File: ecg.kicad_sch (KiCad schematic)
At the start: 37 parts, among them SW1 SW_Push, SW2 SW_Push, U1 ESP32-S3-PICO-1-N8R2, U2 AD620, U3 OPA358, U4 TPS7A8101DRBR

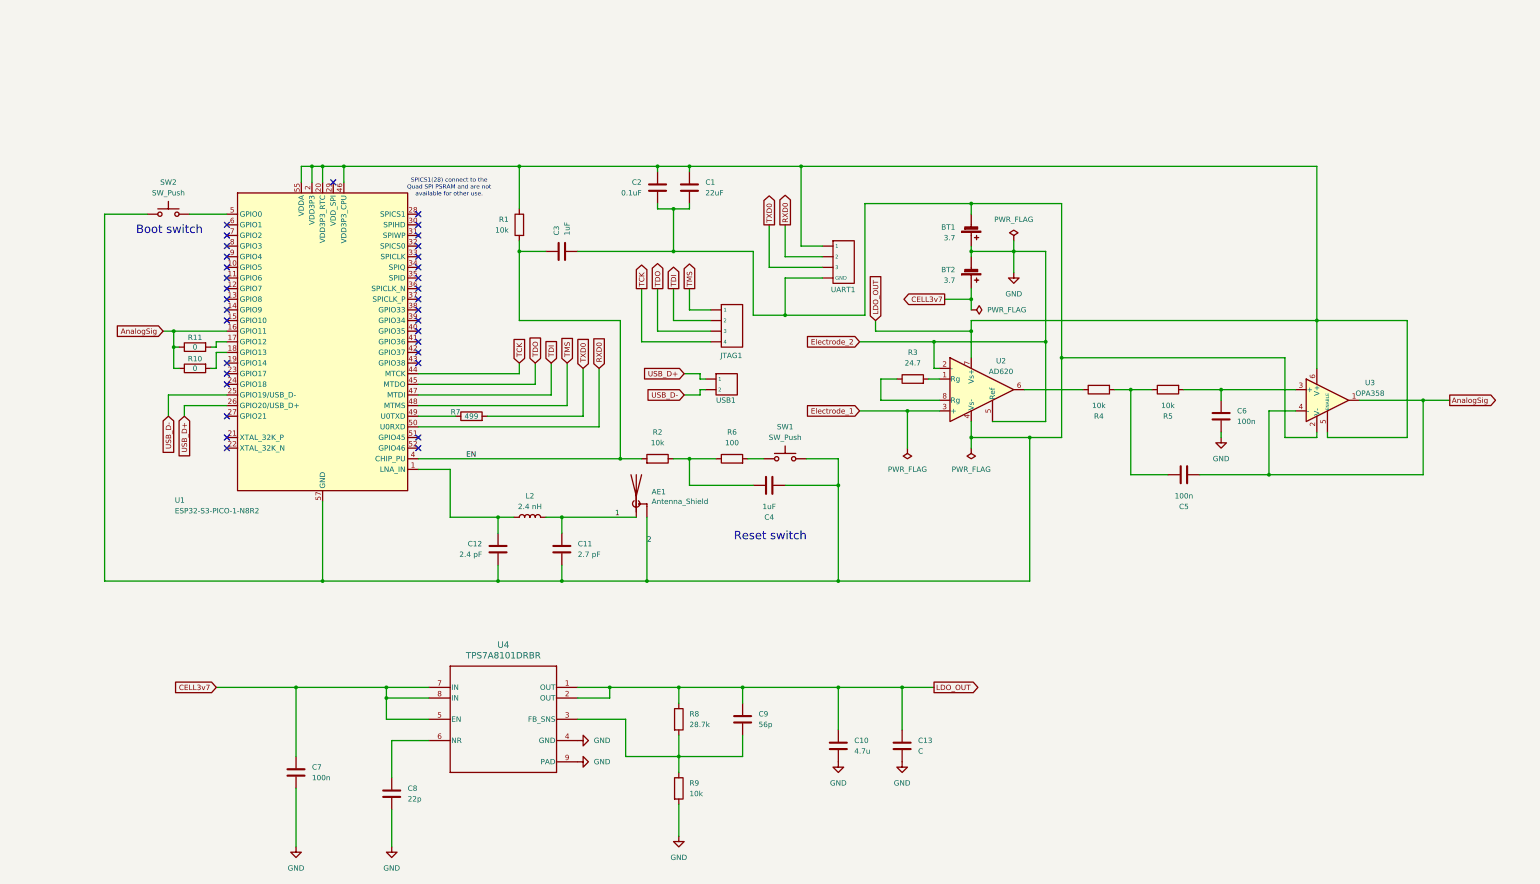
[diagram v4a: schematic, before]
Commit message: Up to date with Final PCB sent for fabrication
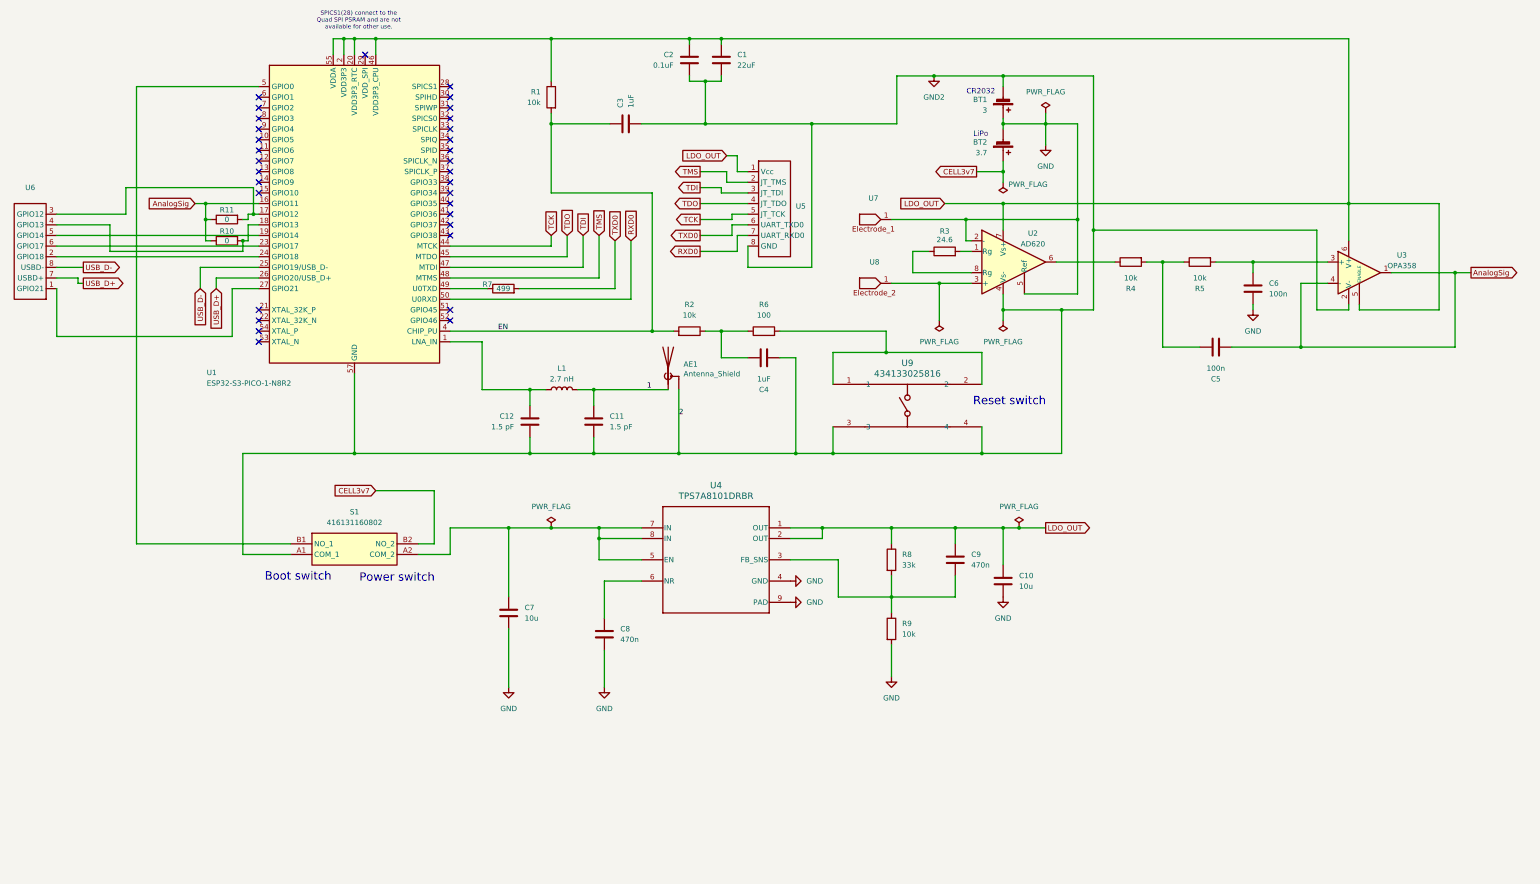
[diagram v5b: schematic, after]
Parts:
- removed C13: C, Capacitor_SMD:C_0201_0603Metric, symbol Device:C
- removed JTAG1: ~, symbol jtag:JTAG_Blackbox
- removed SW1, SW2: SW_Push, Button_Switch_THT:SW_PUSH_6mm_H5mm, symbol Switch:SW_Push
- removed UART1: ~, symbol uart:UART_Blackbox
- removed USB1: ~, symbol usb:USB_Blackbox
- added S1: 416131160802, Slide:416131160802, symbol slide:416131160802
- added U5: ~, Socket:Socket_THT_MountingHoles, symbol JT_USB_UART:JT_USB_UART1
- added U6: ~, Socket:Socket_THT_MountingHoles, symbol JT_USB_UART:JT_USB_UART2
- added U7: ~, Electrode:TestPoint_Pad_1.0x1.0mm, symbol Electrode:Electrode_1
- added U8: ~, Electrode:TestPoint_Pad_1.0x1.0mm, symbol Electrode:Electrode_2
- added U9: 434133025816, Tactile:SMD_025816_WRE, symbol Tactile:434133025816
- AE1: footprint RF_Antenna:Texas_SWRA117D_2.4GHz_Left -> RF_Antenna:Texas_SWRA117D_2.4GHz_Right
- BT1: value 3.7 -> 3; footprint (none) -> CR2032_module:TestPoint_Pad_1.0x1.0mm
- BT2: footprint (none) -> CR2032_module:TestPoint_Pad_1.0x1.0mm
- C1, C2, C3, C4, C5, C6: footprint Capacitor_SMD:C_0201_0603Metric -> Capacitor_SMD:C_0603_1608Metric
- C10: value 4.7u -> 10u; footprint Capacitor_SMD:C_0201_0603Metric -> Capacitor_SMD:C_0603_1608Metric
- C11: value 2.7 pF -> 1.5 pF
- C12: value 2.4 pF -> 1.5 pF
- C7: value 100n -> 10u; footprint Capacitor_SMD:C_0201_0603Metric -> Capacitor_SMD:C_0603_1608Metric
- C8: value 22p -> 470n; footprint Capacitor_SMD:C_0201_0603Metric -> Capacitor_SMD:C_0603_1608Metric
- C9: value 56p -> 470n; footprint Capacitor_SMD:C_0201_0603Metric -> Capacitor_SMD:C_0603_1608Metric
- L1: renamed from L2; value 2.4 nH -> 2.7 nH
- R1, R2, R4, R5, R6, R7, R9: footprint Resistor_SMD:R_0201_0603Metric -> Resistor_SMD:R_0603_1608Metric
- R10, R11: footprint (none) -> Resistor_SMD:R_0603_1608Metric
- R3: value 24.7 -> 24.6; footprint Resistor_SMD:R_0201_0603Metric -> Resistor_SMD:R_0603_1608Metric
- R8: value 28.7k -> 33k; footprint Resistor_SMD:R_0201_0603Metric -> Resistor_SMD:R_0603_1608Metric
- U1: footprint Package_DFN_QFN:QFN-56-1EP_7x7mm_P0.4mm_EP4x4mm -> ESP32_S3_PICO_1_N8R2:QFN56_7X7_EXP
- U4: footprint (none) -> TPS7A8101DRBR:IC_DRV8601DRBT
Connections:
- net CELL3v7: now also S1.B2 (NO_2); no longer C7.1, U4.5 (EN), U4.7 (IN), U4.8 (IN)
- net GND: now also U7.1
- net LDO_OUT: now also U5.1 (Vcc)
- net RXD0: now also U5.7 (UART_RXD0)
- net TCK: now also U5.5 (JT_TCK)
- net TDI: now also U5.3 (JT_TDI)
- net TDO: now also U5.4 (JT_TDO)
- net TMS: now also U5.2 (JT_TMS)
- net TXD0: now also U5.6 (UART_TXD0)
- net USB_D+: now also U6.7 (USBD+)
- net USB_D-: now also U6.8 (USBD-)
- net at U1.5 (GPIO0): now also S1.B1 (NO_1)
- net at R6.2: now also U9.1, U9.2
- net at R10.2, U1.18 (GPIO13): now also U6.4 (GPIO13)
- net at R11.2, U1.17 (GPIO12): now also U6.3 (GPIO12)
- net at U1.19 (GPIO14): now also U6.5 (GPIO14)
- net at U1.23 (GPIO17): now also U6.6 (GPIO17)
- net at U1.24 (GPIO18): now also U6.2 (GPIO18)
- net at U1.27 (GPIO21): now also U6.1 (GPIO21)
- net 2 renamed GND2
- net GND2: now also S1.A1 (COM_1), U5.8 (GND), U9.3, U9.4
- net Electrode_1: no longer names the net of U2.3 (+)
- net Electrode_1: now also U8.1
- new net: C7.1, S1.A2 (COM_2), U4.5 (EN), U4.7 (IN), U4.8 (IN)
- no-connect marks 34 -> 32
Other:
- note added: "CR2032"
- note added: "LiPo"
- note added: "Power switch"
- moved on the sheet: AE1, BT1, BT2, C1, C10, C11, C12, C2, C3, C4, C5, C6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
